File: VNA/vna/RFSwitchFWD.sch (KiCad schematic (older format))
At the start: 2 parts

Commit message: adjusted main schematic to suit initial presentation
i moved a few blocks around so that the cropped version of the block diagram would fit nicely in my semester 1 presentation
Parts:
- removed C1: 10u, symbol Device:C_Small
- removed SWs1: ADG918BRM, Package_SO:MSOP-8_3x3mm_P0.65mm, symbol RF_Switch:ADG918BRM
- added C2: 10u, symbol Device:C_Small
- added SWs2: ADG918BRM, Package_SO:MSOP-8_3x3mm_P0.65mm, symbol RF_Switch:ADG918BRM
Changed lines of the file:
@@
 $Comp
 L RF_Switch:ADG918BRM SWs?
-U 1 1 5CC6F338
+U 1 1 5CE66E3D
 P 5150 2750
-AR Path="/5CC6F338" Ref="SWs?"  Part="1"
-AR Path="/5CC6DDE1/5CC6F338" Ref="SWs1"  Part="1"
-AR Path="/5CCA83E4/5CC6F338" Ref="SWs?"  Part="1"
-AR Path="/5CCA873A/5CC6F338" Ref="SWs?"  Part="1"
-AR Path="/5CCA9268/5CC6F338" Ref="SWs?"  Part="1"
-AR Path="/5CCA993F/5CC6F338" Ref="SWs?"  Part="1"
-F 0 "SWs?" H 4900 3100 50  0000 C CNN
+AR Path="/5CE66E3D" Ref="SWs?"  Part="1"
+AR Path="/5CC6DDE1/5CE66E3D" Ref="SWs?"  Part="1"
+AR Path="/5CCA83E4/5CE66E3D" Ref="SWs2"  Part="1"
+AR Path="/5CCA873A/5CE66E3D" Ref="SWs?"  Part="1"
+AR Path="/5CCA9268/5CE66E3D" Ref="SWs?"  Part="1"
+AR Path="/5CCA993F/5CE66E3D" Ref="SWs?"  Part="1"
+F 0 "SWs2" H 4900 3100 50  0000 C CNN
 F 1 "ADG918BRM" H 5400 3200 50  0000 C CNN
 F 2 "Package_SO:MSOP-8_3x3mm_P0.65mm" H 5150 2300 50  0001 C CNN
@@
 $Comp
 L Device:C_Small C?
-U 1 1 5CC702A7
+U 1 1 5CE66E3E
 P 6400 2600
-AR Path="/5CC702A7" Ref="C?"  Part="1"
-AR Path="/5CC6DDE1/5CC702A7" Ref="C1"  Part="1"
-AR Path="/5CCA83E4/5CC702A7" Ref="C?"  Part="1"
-AR Path="/5CCA873A/5CC702A7" Ref="C?"  Part="1"
-AR Path="/5CCA9268/5CC702A7" Ref="C?"  Part="1"
-AR Path="/5CCA993F/5CC702A7" Ref="C?"  Part="1"
-F 0 "C?" H 6492 2646 50  0000 L CNN
+AR Path="/5CE66E3E" Ref="C?"  Part="1"
+AR Path="/5CC6DDE1/5CE66E3E" Ref="C?"  Part="1"
+AR Path="/5CCA83E4/5CE66E3E" Ref="C2"  Part="1"
+AR Path="/5CCA873A/5CE66E3E" Ref="C?"  Part="1"
+AR Path="/5CCA9268/5CE66E3E" Ref="C?"  Part="1"
+AR Path="/5CCA993F/5CE66E3E" Ref="C?"  Part="1"
+F 0 "C2" H 6492 2646 50  0000 L CNN
 F 1 "10u" H 6492 2555 50  0000 L CNN
 F 2 "" H 6400 2600 50  0001 C CNN
@@
 $Comp
 L power:GNDD #PWR?
-U 1 1 5CCA53F1
+U 1 1 5CE66E3F
 P 5150 3300
-AR Path="/5CC6DDE1/5CCA53F1" Ref="#PWR?"  Part="1"
-AR Path="/5CCA83E4/5CCA53F1" Ref="#PWR?"  Part="1"
-AR Path="/5CCA873A/5CCA53F1" Ref="#PWR?"  Part="1"
-AR Path="/5CCA9268/5CCA53F1" Ref="#PWR?"  Part="1"
-AR Path="/5CCA993F/5CCA53F1" Ref="#PWR?"  Part="1"
-F 0 "#PWR?" H 5150 3050 50  0001 C CNN
+AR Path="/5CC6DDE1/5CE66E3F" Ref="#PWR?"  Part="1"
+AR Path="/5CCA83E4/5CE66E3F" Ref="#PWR012"  Part="1"
+AR Path="/5CCA873A/5CE66E3F" Ref="#PWR?"  Part="1"
+AR Path="/5CCA9268/5CE66E3F" Ref="#PWR?"  Part="1"
+AR Path="/5CCA993F/5CE66E3F" Ref="#PWR?"  Part="1"
+F 0 "#PWR012" H 5150 3050 50  0001 C CNN
 F 1 "GNDD" H 5154 3145 50  0000 C CNN
 F 2 "" H 5150 3300 50  0001 C CNN
@@
 $Comp
 L power:VDD #PWR?
-U 1 1 5CCA5AC1
+U 1 1 5CE66E40
 P 5150 2200
-AR Path="/5CC6DDE1/5CCA5AC1" Ref="#PWR?"  Part="1"
-AR Path="/5CCA83E4/5CCA5AC1" Ref="#PWR?"  Part="1"
-AR Path="/5CCA873A/5CCA5AC1" Ref="#PWR?"  Part="1"
-AR Path="/5CCA9268/5CCA5AC1" Ref="#PWR?"  Part="1"
-AR Path="/5CCA993F/5CCA5AC1" Ref="#PWR?"  Part="1"
-F 0 "#PWR?" H 5150 2050 50  0001 C CNN
+AR Path="/5CC6DDE1/5CE66E40" Ref="#PWR?"  Part="1"
+AR Path="/5CCA83E4/5CE66E40" Ref="#PWR011"  Part="1"
+AR Path="/5CCA873A/5CE66E40" Ref="#PWR?"  Part="1"
+AR Path="/5CCA9268/5CE66E40" Ref="#PWR?"  Part="1"
+AR Path="/5CCA993F/5CE66E40" Ref="#PWR?"  Part="1"
+F 0 "#PWR011" H 5150 2050 50  0001 C CNN
 F 1 "VDD" H 5167 2373 50  0000 C CNN
 F 2 "" H 5150 2200 50  0001 C CNN

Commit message: micro-controller pins labelled
micro controller pins have been labelled, the pins on the bottom are yet to be linked to them.

still to wire up ftdi chip,

still to decide upon rf switch control schema.
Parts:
- renumbered C2 to C12, SWs2 to SWs3
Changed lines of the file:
@@
 AR Path="/5CE66E3D" Ref="SWs?"  Part="1"
 AR Path="/5CC6DDE1/5CE66E3D" Ref="SWs?"  Part="1"
-AR Path="/5CCA83E4/5CE66E3D" Ref="SWs2"  Part="1"
+AR Path="/5CCA83E4/5CE66E3D" Ref="SWs3"  Part="1"
 AR Path="/5CCA873A/5CE66E3D" Ref="SWs?"  Part="1"
 AR Path="/5CCA9268/5CE66E3D" Ref="SWs?"  Part="1"
 AR Path="/5CCA993F/5CE66E3D" Ref="SWs?"  Part="1"
-F 0 "SWs2" H 4900 3100 50  0000 C CNN
+F 0 "SWs3" H 4900 3100 50  0000 C CNN
 F 1 "ADG918BRM" H 5400 3200 50  0000 C CNN
 F 2 "Package_SO:MSOP-8_3x3mm_P0.65mm" H 5150 2300 50  0001 C CNN
@@
 AR Path="/5CE66E3E" Ref="C?"  Part="1"
 AR Path="/5CC6DDE1/5CE66E3E" Ref="C?"  Part="1"
-AR Path="/5CCA83E4/5CE66E3E" Ref="C2"  Part="1"
+AR Path="/5CCA83E4/5CE66E3E" Ref="C12"  Part="1"
 AR Path="/5CCA873A/5CE66E3E" Ref="C?"  Part="1"
 AR Path="/5CCA9268/5CE66E3E" Ref="C?"  Part="1"
 AR Path="/5CCA993F/5CE66E3E" Ref="C?"  Part="1"
-F 0 "C2" H 6492 2646 50  0000 L CNN
+F 0 "C12" H 6492 2646 50  0000 L CNN
 F 1 "10u" H 6492 2555 50  0000 L CNN
 F 2 "" H 6400 2600 50  0001 C CNN
@@
 P 5150 3300
 AR Path="/5CC6DDE1/5CE66E3F" Ref="#PWR?"  Part="1"
-AR Path="/5CCA83E4/5CE66E3F" Ref="#PWR012"  Part="1"
+AR Path="/5CCA83E4/5CE66E3F" Ref="#PWR024"  Part="1"
 AR Path="/5CCA873A/5CE66E3F" Ref="#PWR?"  Part="1"
 AR Path="/5CCA9268/5CE66E3F" Ref="#PWR?"  Part="1"
 AR Path="/5CCA993F/5CE66E3F" Ref="#PWR?"  Part="1"
-F 0 "#PWR012" H 5150 3050 50  0001 C CNN
+F 0 "#PWR024" H 5150 3050 50  0001 C CNN
 F 1 "GNDD" H 5154 3145 50  0000 C CNN
 F 2 "" H 5150 3300 50  0001 C CNN
@@
 P 5150 2200
 AR Path="/5CC6DDE1/5CE66E40" Ref="#PWR?"  Part="1"
-AR Path="/5CCA83E4/5CE66E40" Ref="#PWR011"  Part="1"
+AR Path="/5CCA83E4/5CE66E40" Ref="#PWR023"  Part="1"
 AR Path="/5CCA873A/5CE66E40" Ref="#PWR?"  Part="1"
 AR Path="/5CCA9268/5CE66E40" Ref="#PWR?"  Part="1"
 AR Path="/5CCA993F/5CE66E40" Ref="#PWR?"  Part="1"
-F 0 "#PWR011" H 5150 2050 50  0001 C CNN
+F 0 "#PWR023" H 5150 2050 50  0001 C CNN
 F 1 "VDD" H 5167 2373 50  0000 C CNN
 F 2 "" H 5150 2200 50  0001 C CNN

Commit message: finished controller, chose compatible switches
controller and rf switches have been completed.

ToDo: finish filter design for RF Source, add auto gain control
ToDo: finish directional coupler footprints
ToDo: PCB Layout
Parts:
- removed C12: 10u, symbol Device:C_Small
- removed SWs3: ADG918BRM, Package_SO:MSOP-8_3x3mm_P0.65mm, symbol RF_Switch:ADG918BRM
- added C23, C24, C25: 100n, Capacitor_SMD:C_0805_2012Metric_Pad1.15x1.40mm_HandSolder, symbol Device:C_Small
- added U1: 74HCT04, Package_SO:SOIC-14_3.9x8.7mm_P1.27mm, symbol 74xx:74HCT04
- added U9: HMC284, Package_SO:MSOP-8-1EP_3x3mm_P0.65mm_EP2.5x3mm_Mask1.73x2.36mm_ThermalVias, symbol vna-rescue:HMC284
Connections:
- net labels added: GND
- net labels removed: GNDD, VDD
- wire segments 6 -> 21
- no-connect marks 0 -> 1
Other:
- note added: "Hex Inverter"
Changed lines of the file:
@@
 $Descr A4 11693 8268
 encoding utf-8
-Sheet 5 10
+Sheet 9 10
 Title ""
 Date ""
@@
 Comment4 ""
 $EndDescr
+Text HLabel 6800 3850 2    50   Input ~ 0
+FwdOut
+Text HLabel 7100 1650 2    50   Input ~ 0
+Fwd1In
+Text HLabel 6100 1650 0    50   Input ~ 0
+Fwd2In
+Text HLabel 5000 3550 0    50   Input ~ 0
+Ctrl
 $Comp
-L RF_Switch:ADG918BRM SWs?
-U 1 1 5CE66E3D
-P 5150 2750
-AR Path="/5CE66E3D" Ref="SWs?"  Part="1"
-AR Path="/5CC6DDE1/5CE66E3D" Ref="SWs?"  Part="1"
-AR Path="/5CCA83E4/5CE66E3D" Ref="SWs3"  Part="1"
-AR Path="/5CCA873A/5CE66E3D" Ref="SWs?"  Part="1"
-AR Path="/5CCA9268/5CE66E3D" Ref="SWs?"  Part="1"
-AR Path="/5CCA993F/5CE66E3D" Ref="SWs?"  Part="1"
-F 0 "SWs3" H 4900 3100 50  0000 C CNN
-F 1 "ADG918BRM" H 5400 3200 50  0000 C CNN
-F 2 "Package_SO:MSOP-8_3x3mm_P0.65mm" H 5150 2300 50  0001 C CNN
-F 3 "https://www.analog.com/media/en/technical-documentation/data-sheets/ADG918_919.pdf" H 5100 2950 50  0001 C CNN
-	1    5150 2750
+L vna-rescue:HMC284 U?
+U 1 1 5D85D74F
+P 6650 2800
+AR Path="/5CC6DDE1/5D85D74F" Ref="U?"  Part="1"
+AR Path="/5CCA83E4/5D85D74F" Ref="U9"  Part="1"
+F 0 "U9" H 7028 2871 50  0000 L CNN
+F 1 "HMC284" H 7028 2780 50  0000 L CNN
+F 2 "Package_SO:MSOP-8-1EP_3x3mm_P0.65mm_EP2.5x3mm_Mask1.73x2.36mm_ThermalVias" H 6400 2850 50  0001 C CNN
+F 3 "" H 6400 2850 50  0001 C CNN
+	1    6650 2800
+	1    0    0    -1
+$EndComp
+$Comp
+L power:GND #PWR?
+U 1 1 5D85D755
+P 6650 2050
+AR Path="/5CC6DDE1/5D85D755" Ref="#PWR?"  Part="1"
+AR Path="/5CCA83E4/5D85D755" Ref="#PWR057"  Part="1"
+F 0 "#PWR057" H 6650 1800 50  0001 C CNN
+F 1 "GND" H 6655 1877 50  0000 C CNN
+F 2 "" H 6650 2050 50  0001 C CNN
+F 3 "" H 6650 2050 50  0001 C CNN
+	1    6650 2050
+	1    0    0    -1
+$EndComp
+Wire Wire Line
+	6550 2250 6550 2050
+Wire Wire Line
+	6550 2050 6650 2050
+Wire Wire Line
+	6650 2050 6750 2050
+Wire Wire Line
+	6750 2050 6750 2250
+Connection ~ 6650 2050
+NoConn ~ 6900 3300
+$Comp
+L Device:C_Small C?
+U 1 1 5D85D761
+P 6750 3500
+AR Path="/5CC6DDE1/5D85D761" Ref="C?"  Part="1"
+AR Path="/5CCA83E4/5D85D761" Ref="C25"  Part="1"
+F 0 "C25" H 6842 3546 50  0000 L CNN
+F 1 "100n" H 6842 3455 50  0000 L CNN
+F 2 "Capacitor_SMD:C_0805_2012Metric_Pad1.15x1.40mm_HandSolder" H 6750 3500 50  0001 C CNN
+F 3 "~" H 6750 3500 50  0001 C CNN
+	1    6750 3500
+	1    0    0    -1
+$EndComp
+Wire Wire Line
+	6750 3300 6750 3400
+$Comp
+L Device:C_Small C?
+U 1 1 5D85D769
+P 6100 1950
+AR Path="/5CC6DDE1/5D85D769" Ref="C?"  Part="1"
+AR Path="/5CCA83E4/5D85D769" Ref="C23"  Part="1"
+F 0 "C23" H 6192 1996 50  0000 L CNN
+F 1 "100n" H 6192 1905 50  0000 L CNN
+F 2 "Capacitor_SMD:C_0805_2012Metric_Pad1.15x1.40mm_HandSolder" H 6100 1950 50  0001 C CNN
+F 3 "~" H 6100 1950 50  0001 C CNN
+	1    6100 1950
 	1    0    0    -1
 $EndComp
 $Comp
 L Device:C_Small C?
-U 1 1 5CE66E3E
-P 6400 2600
-AR Path="/5CE66E3E" Ref="C?"  Part="1"
-AR Path="/5CC6DDE1/5CE66E3E" Ref="C?"  Part="1"
-AR Path="/5CCA83E4/5CE66E3E" Ref="C12"  Part="1"
-AR Path="/5CCA873A/5CE66E3E" Ref="C?"  Part="1"
-AR Path="/5CCA9268/5CE66E3E" Ref="C?"  Part="1"
-AR Path="/5CCA993F/5CE66E3E" Ref="C?"  Part="1"
-F 0 "C12" H 6492 2646 50  0000 L CNN
-F 1 "10u" H 6492 2555 50  0000 L CNN
-F 2 "" H 6400 2600 50  0001 C CNN
-F 3 "~" H 6400 2600 50  0001 C CNN
-	1    6400 2600
+U 1 1 5D85D76F
+P 7100 1950
+AR Path="/5CC6DDE1/5D85D76F" Ref="C?"  Part="1"
+AR Path="/5CCA83E4/5D85D76F" Ref="C24"  Part="1"
+F 0 "C24" H 7192 1996 50  0000 L CNN
+F 1 "100n" H 7192 1905 50  0000 L CNN
+F 2 "Capacitor_SMD:C_0805_2012Metric_Pad1.15x1.40mm_HandSolder" H 7100 1950 50  0001 C CNN
+F 3 "~" H 7100 1950 50  0001 C CNN
+	1    7100 1950
 	1    0    0    -1
 $EndComp
-Text HLabel 4650 2650 0    50   Input ~ 0
-FwdOut
-Text HLabel 5650 2550 2    50   Input ~ 0
-Fwd1In
-Text HLabel 5650 2750 2    50   Input ~ 0
-Fwd2In
+Wire Wire Line
+	6900 2250 7100 2250
+Wire Wire Line
+	7100 2250 7100 2050
+Wire Wire Line
+	6400 2250 6100 2250
+Wire Wire Line
+	6100 2250 6100 2050
+Wire Wire Line
+	6100 1850 6100 1650
 $Comp
-L power:GNDD #PWR?
-U 1 1 5CE66E3F
-P 5150 3300
-AR Path="/5CC6DDE1/5CE66E3F" Ref="#PWR?"  Part="1"
-AR Path="/5CCA83E4/5CE66E3F" Ref="#PWR024"  Part="1"
-AR Path="/5CCA873A/5CE66E3F" Ref="#PWR?"  Part="1"
-AR Path="/5CCA9268/5CE66E3F" Ref="#PWR?"  Part="1"
-AR Path="/5CCA993F/5CE66E3F" Ref="#PWR?"  Part="1"
-F 0 "#PWR024" H 5150 3050 50  0001 C CNN
-F 1 "GNDD" H 5154 3145 50  0000 C CNN
-F 2 "" H 5150 3300 50  0001 C CNN
-F 3 "" H 5150 3300 50  0001 C CNN
-	1    5150 3300
+L 74xx:74HCT04 U?
+U 3 1 5D85D77B
+P 5500 3550
+AR Path="/5CC6DDE1/5D85D77B" Ref="U?"  Part="1"
+AR Path="/5CCA83E4/5D85D77B" Ref="U1"  Part="3"
+F 0 "U1" H 5500 3400 50  0000 C CNN
+F 1 "74HCT04" H 5500 3300 50  0000 C CNN
+F 2 "Package_SO:SOIC-14_3.9x8.7mm_P1.27mm" H 5500 3550 50  0001 C CNN
+F 3 "https://assets.nexperia.com/documents/data-sheet/74HC_HCT04.pdf" H 5500 3550 50  0001 C CNN
+	3    5500 3550
 	1    0    0    -1
 $EndComp
 $Comp
-L power:VDD #PWR?
-U 1 1 5CE66E40
-P 5150 2200
-AR Path="/5CC6DDE1/5CE66E40" Ref="#PWR?"  Part="1"
-AR Path="/5CCA83E4/5CE66E40" Ref="#PWR023"  Part="1"
-AR Path="/5CCA873A/5CE66E40" Ref="#PWR?"  Part="1"
-AR Path="/5CCA9268/5CE66E40" Ref="#PWR?"  Part="1"
-AR Path="/5CCA993F/5CE66E40" Ref="#PWR?"  Part="1"
-F 0 "#PWR023" H 5150 2050 50  0001 C CNN
-F 1 "VDD" H 5167 2373 50  0000 C CNN
-F 2 "" H 5150 2200 50  0001 C CNN
-F 3 "" H 5150 2200 50  0001 C CNN
-	1    5150 2200
+L 74xx:74HCT04 U?
+U 4 1 5D85D781
+P 6150 4200
+AR Path="/5CC6DDE1/5D85D781" Ref="U?"  Part="2"
+AR Path="/5CCA83E4/5D85D781" Ref="U1"  Part="4"
+F 0 "U1" H 6150 4517 50  0000 C CNN
+F 1 "74HCT04" H 6150 4426 50  0000 C CNN
+F 2 "Package_SO:SOIC-14_3.9x8.7mm_P1.27mm" H 6150 4200 50  0001 C CNN
+F 3 "https://assets.nexperia.com/documents/data-sheet/74HC_HCT04.pdf" H 6150 4200 50  0001 C CNN
+	4    6150 4200
 	1    0    0    -1
 $EndComp
-Text HLabel 4650 2850 0    50   Input ~ 0
-Ctrl
 Wire Wire Line
-	5150 2200 6400 2200
+	5800 3550 5800 3800
 Wire Wire Line
-	6400 2200 6400 2500
+	5800 4200 5850 4200
 Wire Wire Line
-	5150 2200 5150 2250
-Connection ~ 5150 2200
+	5800 3800 6400 3800
 Wire Wire Line
-	5150 3250 5150 3300
+	6400 3800 6400 3300
+Connection ~ 5800 3800
 Wire Wire Line
-	5150 3300 6400 3300
+	5800 3800 5800 4200
 Wire Wire Line
-	6400 2700 6400 3300
-Connection ~ 5150 3300
-Text GLabel 5800 2200 1    50   Input ~ 0
-VDD
-Text GLabel 5800 3300 3    50   Input ~ 0
-GNDD
+	6450 4200 6550 4200
+Wire Wire Line
+	6550 4200 6550 3300
+Wire Wire Line
+	5000 3550 5200 3550
+Wire Wire Line
+	7100 1850 7100 1650
+Wire Wire Line
+	6750 3850 6800 3850
+Wire Wire Line
+	6750 3600 6750 3850
+Text Notes 5200 4050 0    50   ~ 0
+Hex Inverter
+Wire Notes Line
+	5050 3350 5050 4450
+Wire Notes Line
+	5050 4450 6600 4450
+Wire Notes Line
+	6600 4450 6600 3350
+Wire Notes Line
+	6600 3350 5050 3350
 $EndSCHEMATC

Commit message: custom footprint for couplers, added decoupling caps
added custom footprint for directional couplers - will need to verify it

added decoupling caps to ad9851
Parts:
- C23, C24, C25: footprint Capacitor_SMD:C_0805_2012Metric_Pad1.15x1.40mm_HandSolder -> Capacitor_SMD:C_1206_3216Metric_Pad1.42x1.75mm_HandSolder
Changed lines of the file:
@@
 F 0 "C25" H 6842 3546 50  0000 L CNN
 F 1 "100n" H 6842 3455 50  0000 L CNN
-F 2 "Capacitor_SMD:C_0805_2012Metric_Pad1.15x1.40mm_HandSolder" H 6750 3500 50  0001 C CNN
+F 2 "Capacitor_SMD:C_1206_3216Metric_Pad1.42x1.75mm_HandSolder" H 6750 3500 50  0001 C CNN
 F 3 "~" H 6750 3500 50  0001 C CNN
 	1    6750 3500
@@
 F 0 "C23" H 6192 1996 50  0000 L CNN
 F 1 "100n" H 6192 1905 50  0000 L CNN
-F 2 "Capacitor_SMD:C_0805_2012Metric_Pad1.15x1.40mm_HandSolder" H 6100 1950 50  0001 C CNN
+F 2 "Capacitor_SMD:C_1206_3216Metric_Pad1.42x1.75mm_HandSolder" H 6100 1950 50  0001 C CNN
 F 3 "~" H 6100 1950 50  0001 C CNN
 	1    6100 1950
@@
 F 0 "C24" H 7192 1996 50  0000 L CNN
 F 1 "100n" H 7192 1905 50  0000 L CNN
-F 2 "Capacitor_SMD:C_0805_2012Metric_Pad1.15x1.40mm_HandSolder" H 7100 1950 50  0001 C CNN
+F 2 "Capacitor_SMD:C_1206_3216Metric_Pad1.42x1.75mm_HandSolder" H 7100 1950 50  0001 C CNN
 F 3 "~" H 7100 1950 50  0001 C CNN
 	1    7100 1950

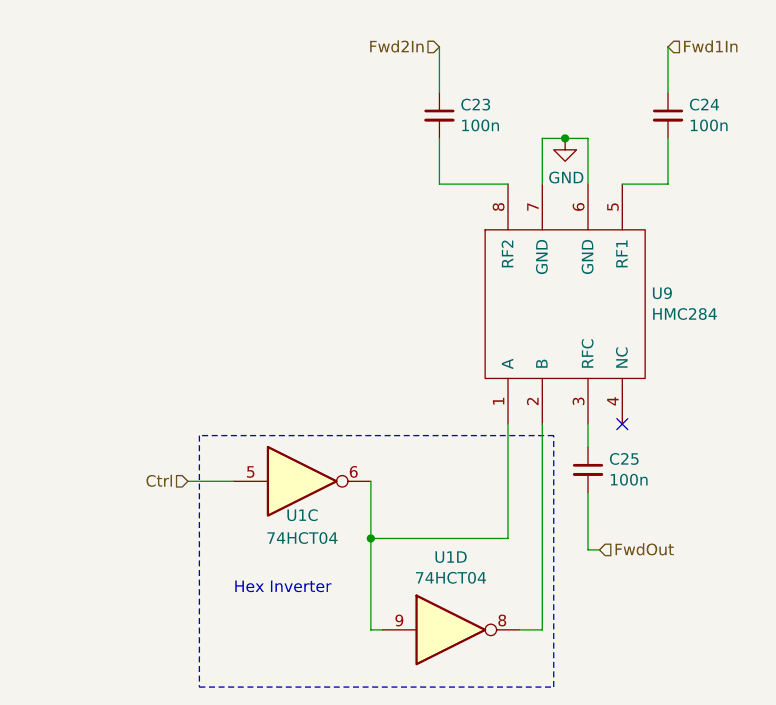
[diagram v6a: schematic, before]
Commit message: initial pcb design
initial layout and grouping of components complete
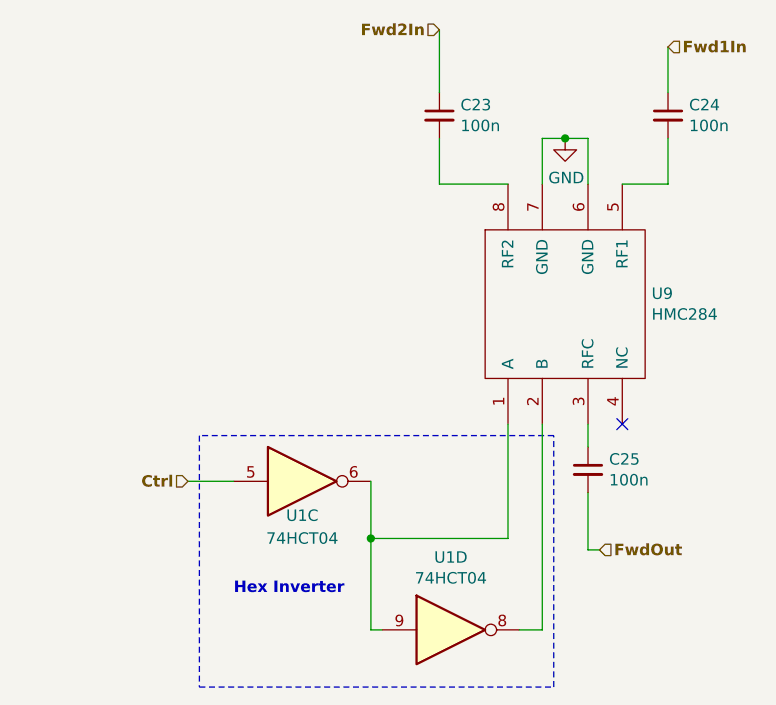
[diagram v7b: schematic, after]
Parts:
- C23, C24, C25: footprint Capacitor_SMD:C_1206_3216Metric_Pad1.42x1.75mm_HandSolder -> Capacitor_SMD:C_0805_2012Metric_Pad1.15x1.40mm_HandSolder
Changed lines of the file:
@@
 $Descr A4 11693 8268
 encoding utf-8
-Sheet 9 10
-Title ""
-Date ""
-Rev ""
-Comp ""
+Sheet 8 10
+Title "Fwd Switch"
+Date "2019-09-25"
+Rev "0.1"
+Comp "Benjamin Jackson"
 Comment1 ""
 Comment2 ""
@@
 Comment4 ""
 $EndDescr
-Text HLabel 6800 3850 2    50   Input ~ 0
+Text HLabel 6800 3850 2    50   Input ~ 10
 FwdOut
-Text HLabel 7100 1650 2    50   Input ~ 0
+Text HLabel 7100 1650 2    50   Input ~ 10
 Fwd1In
-Text HLabel 6100 1650 0    50   Input ~ 0
+Text HLabel 6100 1575 0    50   Input ~ 10
 Fwd2In
-Text HLabel 5000 3550 0    50   Input ~ 0
+Text HLabel 5000 3550 0    50   Input ~ 10
 Ctrl
 $Comp
@@
 F 0 "C25" H 6842 3546 50  0000 L CNN
 F 1 "100n" H 6842 3455 50  0000 L CNN
-F 2 "Capacitor_SMD:C_1206_3216Metric_Pad1.42x1.75mm_HandSolder" H 6750 3500 50  0001 C CNN
+F 2 "Capacitor_SMD:C_0805_2012Metric_Pad1.15x1.40mm_HandSolder" H 6750 3500 50  0001 C CNN
 F 3 "~" H 6750 3500 50  0001 C CNN
 	1    6750 3500
@@
 F 0 "C23" H 6192 1996 50  0000 L CNN
 F 1 "100n" H 6192 1905 50  0000 L CNN
-F 2 "Capacitor_SMD:C_1206_3216Metric_Pad1.42x1.75mm_HandSolder" H 6100 1950 50  0001 C CNN
+F 2 "Capacitor_SMD:C_0805_2012Metric_Pad1.15x1.40mm_HandSolder" H 6100 1950 50  0001 C CNN
 F 3 "~" H 6100 1950 50  0001 C CNN
 	1    6100 1950
@@
 F 0 "C24" H 7192 1996 50  0000 L CNN
 F 1 "100n" H 7192 1905 50  0000 L CNN
-F 2 "Capacitor_SMD:C_1206_3216Metric_Pad1.42x1.75mm_HandSolder" H 7100 1950 50  0001 C CNN
+F 2 "Capacitor_SMD:C_0805_2012Metric_Pad1.15x1.40mm_HandSolder" H 7100 1950 50  0001 C CNN
 F 3 "~" H 7100 1950 50  0001 C CNN
 	1    7100 1950
@@
 Wire Wire Line
 	6100 2250 6100 2050
-Wire Wire Line
-	6100 1850 6100 1650
 $Comp
 L 74xx:74HCT04 U?
@@
 Wire Wire Line
 	6750 3600 6750 3850
-Text Notes 5200 4050 0    50   ~ 0
+Text Notes 5200 4050 0    50   ~ 10
 Hex Inverter
 Wire Notes Line
@@
 Wire Notes Line
 	6600 3350 5050 3350
+Wire Wire Line
+	6100 1575 6100 1850
 $EndSCHEMATC

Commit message: v0.1 completed, producing gerbers
gerbers to be sent to jlc pcb pending their acceptance, they will be produced
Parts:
- U1: footprint Package_SO:SOIC-14_3.9x8.7mm_P1.27mm -> Package_DIP:DIP-14_W10.16mm
- U9: footprint Package_SO:MSOP-8-1EP_3x3mm_P0.65mm_EP2.5x3mm_Mask1.73x2.36mm_ThermalVias -> Package_SO:MSOP-8-1EP_3x3mm_P0.65mm_EP2.5x3mm_Mask1.73x2.36mm
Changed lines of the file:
@@
 F 0 "U9" H 7028 2871 50  0000 L CNN
 F 1 "HMC284" H 7028 2780 50  0000 L CNN
-F 2 "Package_SO:MSOP-8-1EP_3x3mm_P0.65mm_EP2.5x3mm_Mask1.73x2.36mm_ThermalVias" H 6400 2850 50  0001 C CNN
+F 2 "Package_SO:MSOP-8-1EP_3x3mm_P0.65mm_EP2.5x3mm_Mask1.73x2.36mm" H 6400 2850 50  0001 C CNN
 F 3 "" H 6400 2850 50  0001 C CNN
 	1    6650 2800
@@
 F 0 "U1" H 5500 3400 50  0000 C CNN
 F 1 "74HCT04" H 5500 3300 50  0000 C CNN
-F 2 "Package_SO:SOIC-14_3.9x8.7mm_P1.27mm" H 5500 3550 50  0001 C CNN
+F 2 "Package_DIP:DIP-14_W10.16mm" H 5500 3550 50  0001 C CNN
 F 3 "https://assets.nexperia.com/documents/data-sheet/74HC_HCT04.pdf" H 5500 3550 50  0001 C CNN
 	3    5500 3550
@@
 F 0 "U1" H 6150 4517 50  0000 C CNN
 F 1 "74HCT04" H 6150 4426 50  0000 C CNN
-F 2 "Package_SO:SOIC-14_3.9x8.7mm_P1.27mm" H 6150 4200 50  0001 C CNN
+F 2 "Package_DIP:DIP-14_W10.16mm" H 6150 4200 50  0001 C CNN
 F 3 "https://assets.nexperia.com/documents/data-sheet/74HC_HCT04.pdf" H 6150 4200 50  0001 C CNN
 	4    6150 4200
